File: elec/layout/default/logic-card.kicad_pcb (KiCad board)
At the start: 2 copper layers, 76 x 68 mm, 53 parts

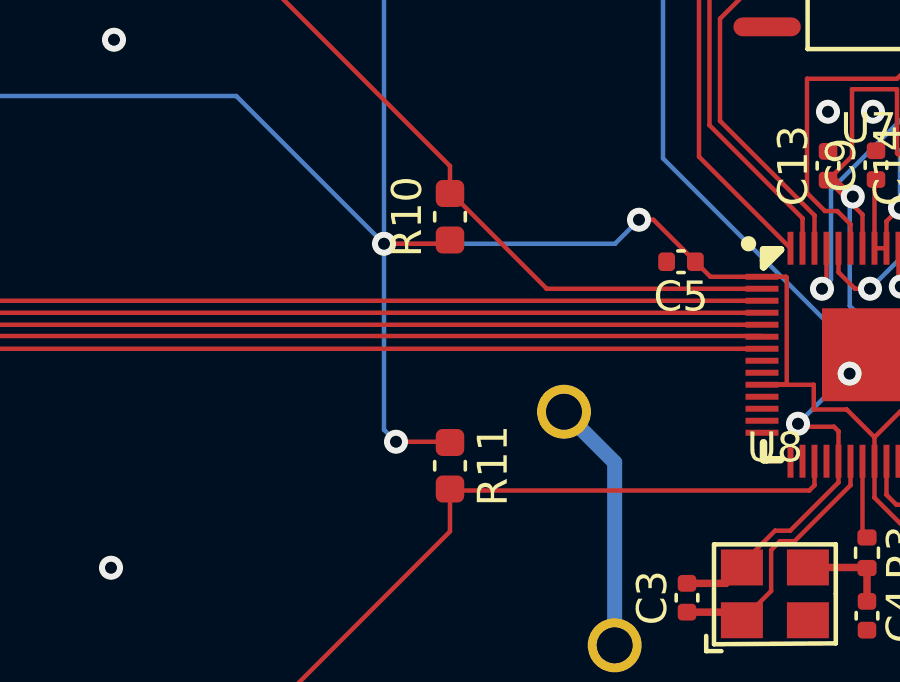
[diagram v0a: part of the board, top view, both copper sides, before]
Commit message: Fix fp-lib-table and UUIDs
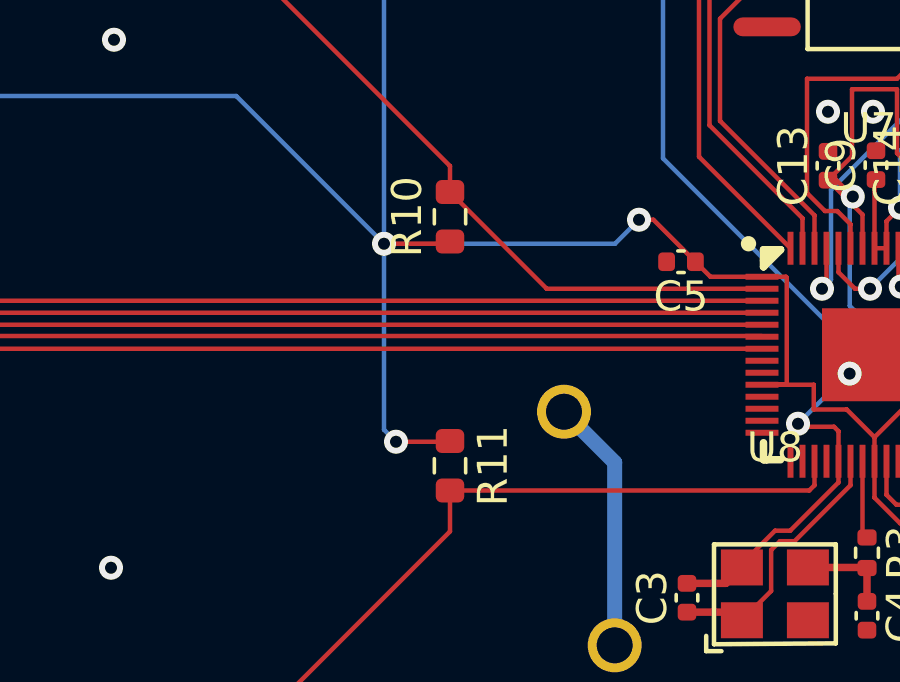
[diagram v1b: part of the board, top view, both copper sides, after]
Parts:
- C1, C10, C14, C2: value 1.0 uF -> Multilayer Ceramic Capacitors MLCC - SMD/SMT 1uF 6.3V 0402 RoHS
- C11, C12, C13, C5, C6, C7, C8, C9: value 100.0 nF -> Multilayer Ceramic Capacitors MLCC - SMD/SMT 100nF 10V 0402 RoHS
- C3, C4: value 22.0 pF -> Multilayer Ceramic Capacitors MLCC - SMD/SMT 20pF 50V 0402 RoHS
- R1: value 18.0 KΩ -> Chip Resistor - Surface Mount 18KOhms ±5% 1/16W 0402 RoHS
- R10, R11: value 10.0 KΩ -> Chip Resistor - Surface Mount 10KOhms ±5% 1/10W 0603 RoHS; footprint lib:C0603 -> lib:R0603
- R12, R13, R14, R15, R16, R2, R6, R7: value 10.0 KΩ -> Chip Resistor - Surface Mount 11KOhms ±5% 1/16W 0402 RoHS
- R17: value 1.5 KΩ -> Chip Resistor - Surface Mount 1.3KOhms ±5% 1/10W 0603 RoHS
- R18, R19: value 100.0 Ω -> Chip Resistor - Surface Mount 91Ohms ±5% 1/10W 0603 RoHS
- R3: value 1.0 KΩ -> Chip Resistor - Surface Mount 1.1KOhms ±5% 1/16W 0402 RoHS
- R4, R5: value 27.0 Ω -> Chip Resistor - Surface Mount 27KOhms ±5% 1/16W 0402 RoHS
- R8, R9: value 4.7 KΩ -> Chip Resistor - Surface Mount 4.7KOhms ±5% 1/16W 0402 RoHS
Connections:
- C3 pad 1: xin -> vcc-4
- C4 pad 1: out-1 -> vcc-5
- R3 pad 2: out-1 -> vcc-5
- U12 pad A4: vcc-4 -> vcc-6
- U12 pad A9: vcc-4 -> vcc-6
- U12 pad B4: vcc-4 -> vcc-6
- U12 pad B9: vcc-4 -> vcc-6
- U13 pad 2: vcc-4 -> vcc-6
- U16 pad 8: out-2 -> out-1
- U7 pad 20: xin -> vcc-4
- U8 pad 1: xin -> vcc-4
- U8 pad 3: out-1 -> vcc-5
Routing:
- net vcc-6: track 0.00 -> 11.3 mm
- net xin: track 9.03 -> 0.00 mm
- net vcc-5: track 0.00 -> 3.09 mm
- net out-1: track 3.09 -> 0.00 mm
- net vcc-4: track 11.3 -> 9.03 mm
